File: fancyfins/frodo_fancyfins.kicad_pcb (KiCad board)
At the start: 2 copper layers, 140 x 115 mm, 102 parts, among them J3 TC2050, U1 AZ1117-5.0, U10 L78L05_SOT89, U11 W25Q128JVP, U12 L78L05_SOT89, U13 L78L05_SOT89, U14 L78L05_SOT89, U15 L78L05_SOT89, U16 L78L05_SOT89, U2 AZ1117-3.3, U3 STM32F103RCTx, U4 MCP2562-E-SN, U5 TPD4E1U06, U6 L78L05_SOT89, U7 L78L05_SOT89, U8 L78L05_SOT89, U9 L78L05_SOT89, Y1 8MHz 12pF

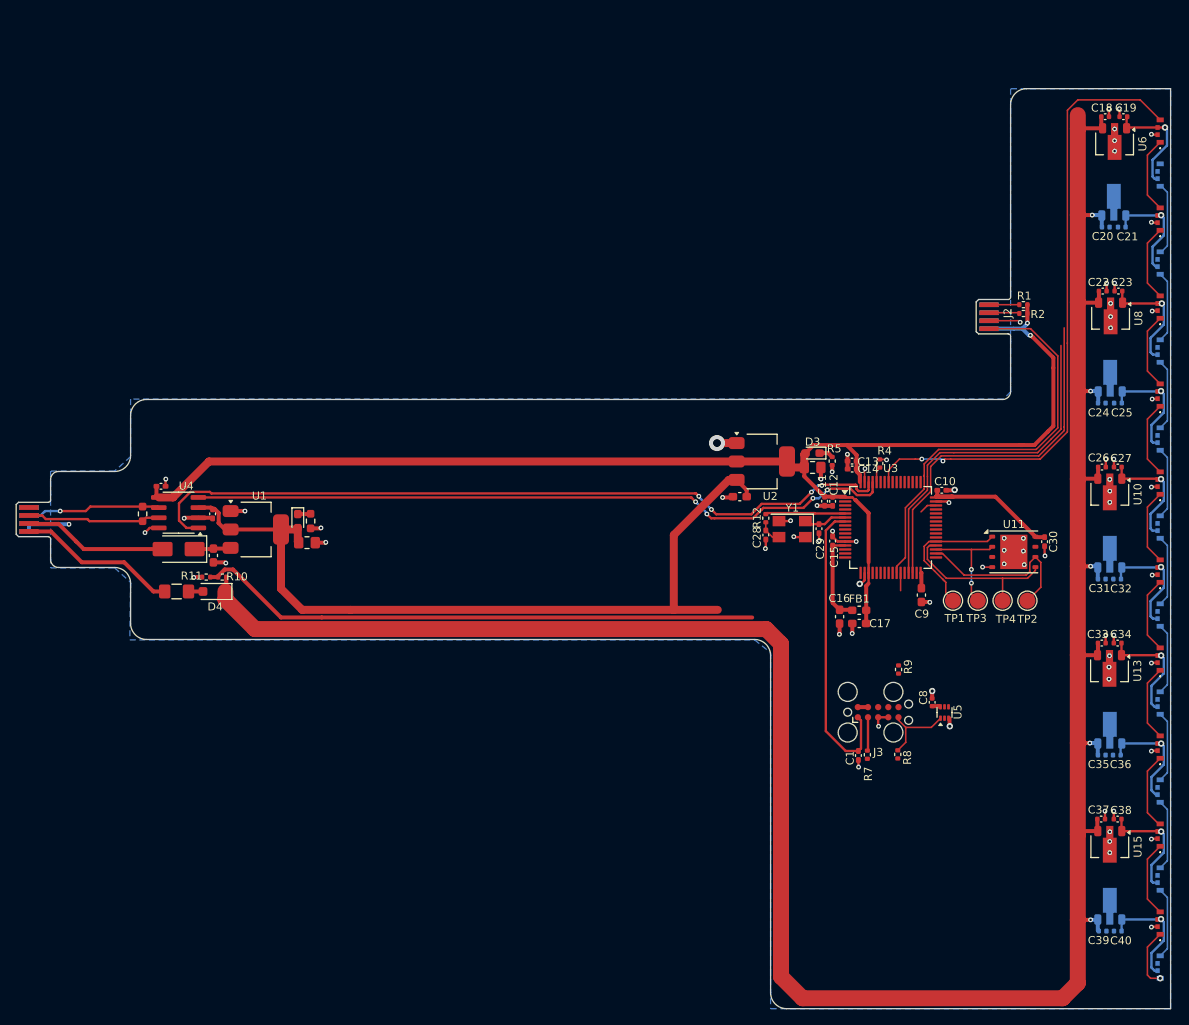
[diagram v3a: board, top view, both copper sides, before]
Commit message: fixed gnd issue
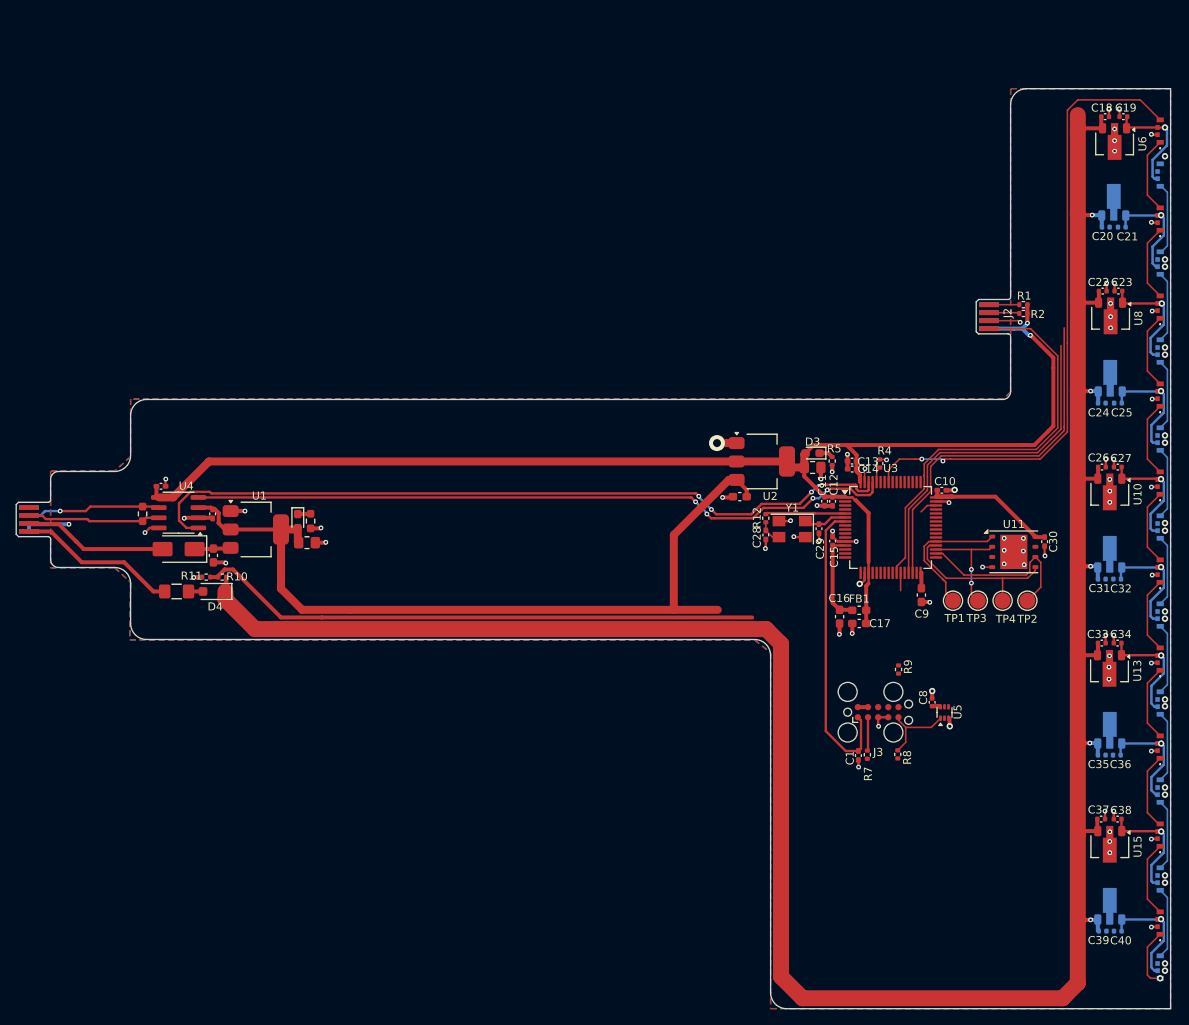
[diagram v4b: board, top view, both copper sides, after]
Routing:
- net GND: vias 77 -> 96
- added copper zone on F.Cu, net GND
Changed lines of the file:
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@@
 	)
 	(via
+		(at 225.3 78.35)
+		(size 0.8)
+		(drill 0.4)
+		(layers "F.Cu" "B.Cu")
+		(free yes)
+		(net 1)
+	)
+	(via
 		(at 169.3 79.3)
 		(size 2)
@@
 	)
 	(via
+		(at 225.3 67.35)
+		(size 0.8)
+		(drill 0.4)
+		(layers "F.Cu" "B.Cu")
+		(free yes)
+		(net 1)
+	)
+	(via
 		(at 223.7 62.8)
 		(size 0.6)
@@
 	)
 	(via
+		(at 225.3 79.25)
+		(size 0.8)
+		(drill 0.4)
+		(layers "F.Cu" "B.Cu")
+		(free yes)
+		(net 1)
+	)
+	(via
 		(at 223.6 139.8)
 		(size 0.6)
@@
 	)
 	(via
+		(at 225.3 101.25)
+		(size 0.8)
+		(drill 0.4)
+		(layers "F.Cu" "B.Cu")
+		(free yes)
+		(net 1)
+	)
+	(via
+		(at 225.3 56.35)
+		(size 0.8)
+		(drill 0.4)
+		(layers "F.Cu" "B.Cu")
+		(free yes)
+		(net 1)
+	)
+	(via
 		(at 218.5 64.9)
 		(size 0.6)
@@
 	)
 	(via
+		(at 225.3 112.2)
+		(size 0.8)
+		(drill 0.4)
+		(layers "F.Cu" "B.Cu")
+		(free yes)
+		(net 1)
+	)
+	(via
 		(at 181.8 87.1)
 		(size 0.6)
@@
 	)
 	(via
+		(at 225.3 122.35)
+		(size 0.8)
+		(drill 0.4)
+		(layers "F.Cu" "B.Cu")
+		(free yes)
+		(net 1)
+	)
+	(via
 		(at 119.8 89.9)
 		(size 0.6)
@@
 	)
 	(via
+		(at 225.3 133.35)
+		(size 0.8)
+		(drill 0.4)
+		(layers "F.Cu" "B.Cu")
+		(free yes)
+		(net 1)
+	)
+	(via
 		(at 218.5 63.5)
 		(size 0.6)
@@
 	)
 	(via
+		(at 225.3 144.35)
+		(size 0.8)
+		(drill 0.4)
+		(layers "F.Cu" "B.Cu")
+		(free yes)
+		(net 1)
+	)
+	(via
 		(at 205.2 94.4)
 		(size 0.6)
@@
 	)
 	(via
+		(at 225.3 134.25)
+		(size 0.8)
+		(drill 0.4)
+		(layers "F.Cu" "B.Cu")
+		(free yes)
+		(net 1)
+	)
+	(via
 		(at 223.6 128.8)
 		(size 0.6)
@@
 	)
 	(via
+		(at 225.3 145.25)
+		(size 0.8)
+		(drill 0.4)
+		(layers "F.Cu" "B.Cu")
+		(free yes)
+		(net 1)
+	)
+	(via
 		(at 100.4 83.8)
 		(size 0.6)
@@
 	)
 	(via
+		(at 225.3 57.25)
+		(size 0.8)
+		(drill 0.4)
+		(layers "F.Cu" "B.Cu")
+		(free yes)
+		(net 1)
+	)
+	(via
 		(at 207.6 92.8)
 		(size 0.6)
@@
 	)
 	(via
+		(at 225.3 111.35)
+		(size 0.8)
+		(drill 0.4)
+		(layers "F.Cu" "B.Cu")
+		(free yes)
+		(net 1)
+	)
+	(via
 		(at 223.7 73.8)
 		(size 0.6)
@@
 	)
 	(via
+		(at 225.3 89.3)
+		(size 0.8)
+		(drill 0.4)
+		(layers "F.Cu" "B.Cu")
+		(free yes)
+		(net 1)
+	)
+	(via
 		(at 107.9 94.3)
 		(size 0.6)
@@
 	)
 	(via
+		(at 225.3 43.45)
+		(size 0.8)
+		(drill 0.4)
+		(layers "F.Cu" "B.Cu")
+		(free yes)
+		(net 1)
+	)
+	(via
 		(at 218.9 81.3)
 		(size 0.6)
@@
 	)
 	(via
+		(at 225.3 100.35)
+		(size 0.8)
+		(drill 0.4)
+		(layers "F.Cu" "B.Cu")
+		(free yes)
+		(net 1)
+	)
+	(via
 		(at 189.5 114.7)
 		(size 0.6)
@@
 	)
 	(via
+		(at 225.3 68.25)
+		(size 0.8)
+		(drill 0.4)
+		(layers "F.Cu" "B.Cu")
+		(free yes)
+		(net 1)
+	)
+	(via
 		(at 207.6 91.2)
 		(size 0.6)
@@
 	)
 	(via
+		(at 225.3 123.25)
+		(size 0.8)
+		(drill 0.4)
+		(layers "F.Cu" "B.Cu")
+		(free yes)
+		(net 1)
+	)
+	(via
+		(at 225.3 90.25)
+		(size 0.8)
+		(drill 0.4)
+		(layers "F.Cu" "B.Cu")
+		(free yes)
+		(net 1)
+	)
+	(via
 		(at 218.4 130.5)
 		(size 0.6)
@@
 		(net 1)
 		(net_name "GND")
+		(layer "F.Cu")
+		(hatch edge 0.5)
+		(priority 1)
+		(connect_pads
+			(clearance 0.25)
+		)
+		(min_thickness 0.25)
+		(filled_areas_thickness no)
+		(fill yes
+			(thermal_gap 0.5)
+			(thermal_bridge_width 0.5)
+			(island_removal_mode 2)
+			(island_area_min 1)
+		)
+		(polygon
+			(pts
+				(xy 86 82.8) (xy 86 94.9) (xy 94 94.85) (xy 96 96.7) (xy 95.9 103.9) (xy 174 103.9) (xy 176 105.5)
+				(xy 176 150) (xy 226.001 150) (xy 226.001 35) (xy 206 35) (xy 206 72.9) (xy 205.1 73.8) (xy 96 73.8)
+				(xy 96 81) (xy 94 82.8)
+			)
+		)
+	)
+	(zone
+		(net 1)
+		(net_name "GND")
 		(layer "B.Cu")
 		(hatch edge 0.5)
 		(connect_pads yes
-			(clearance 0.35)
+			(clearance 0.25)
 		)
 		(min_thickness 0.25)
@@
 			(thermal_gap 0.5)
 			(thermal_bridge_width 0.5)
+			(island_removal_mode 2)
+			(island_area_min 1)
 		)
 		(polygon

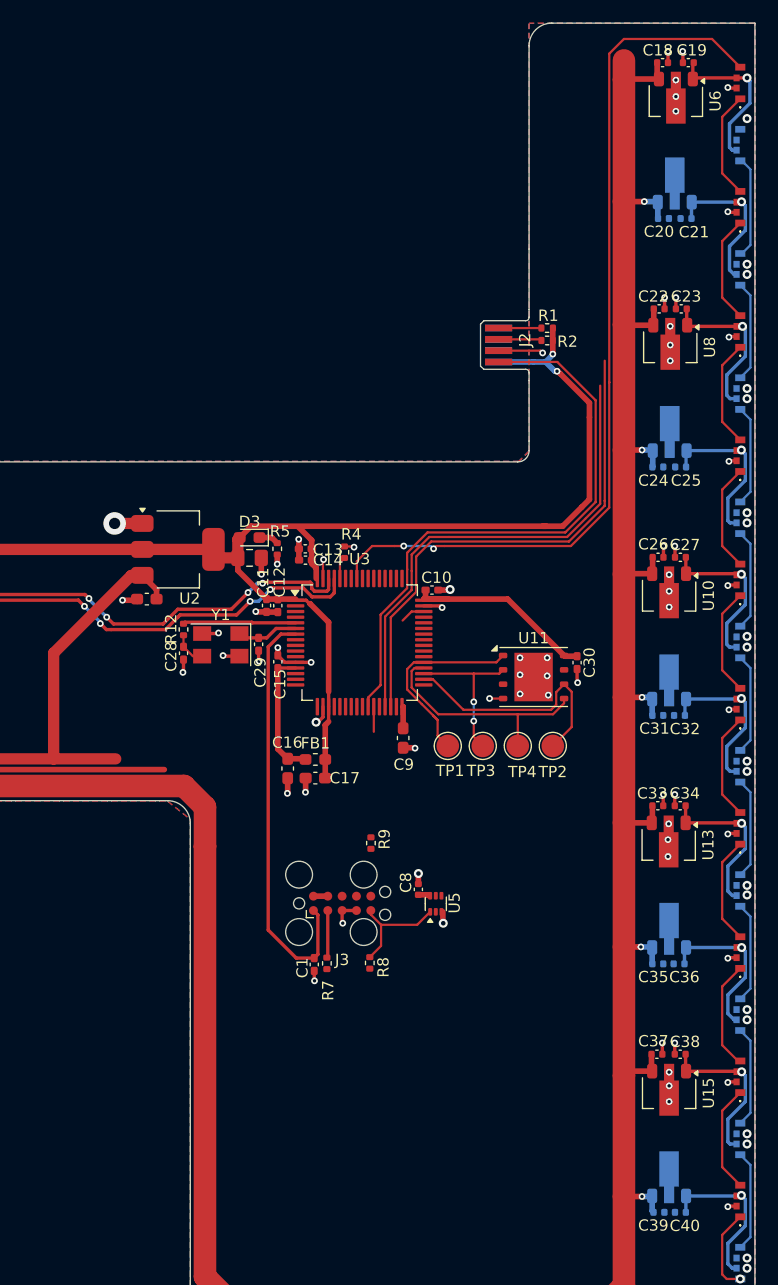
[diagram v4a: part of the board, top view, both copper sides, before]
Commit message: added some vias for better gnd connection
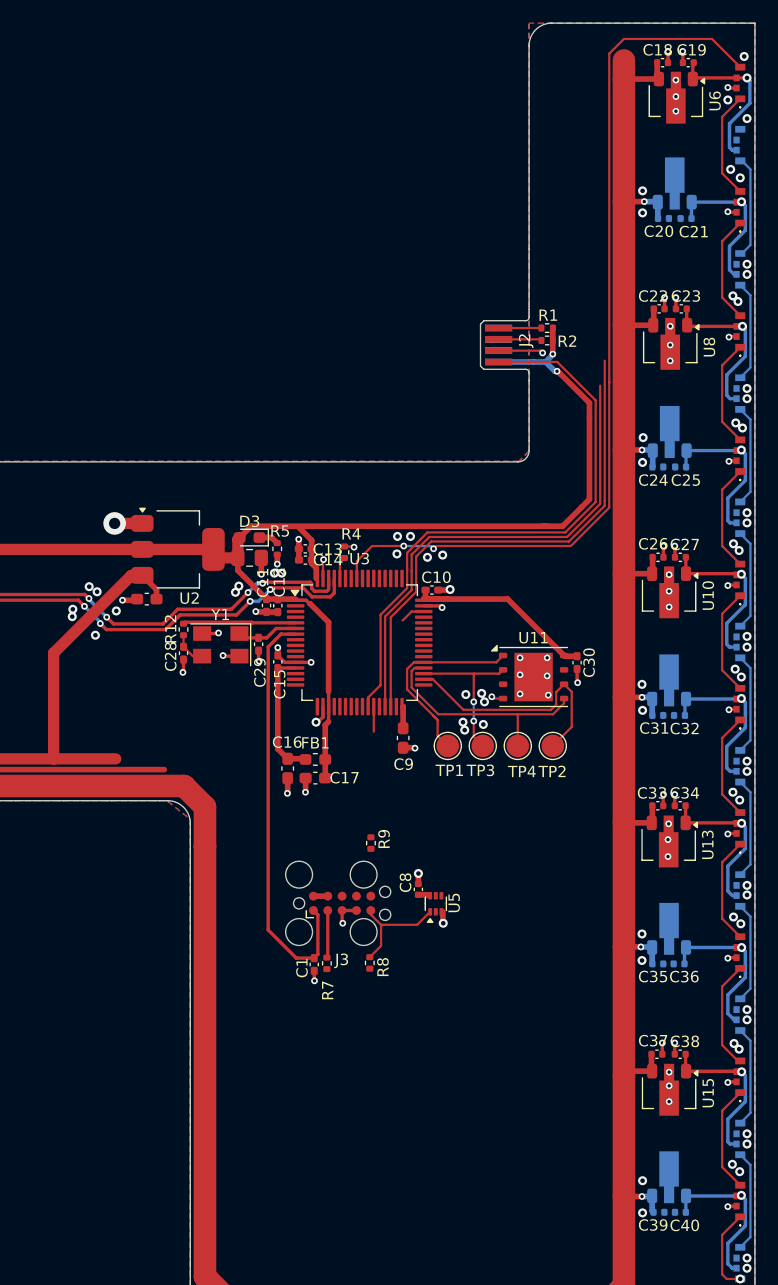
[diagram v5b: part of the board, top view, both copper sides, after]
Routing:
- net GND: track 78.7 -> 78.6 mm, vias 96 -> 147

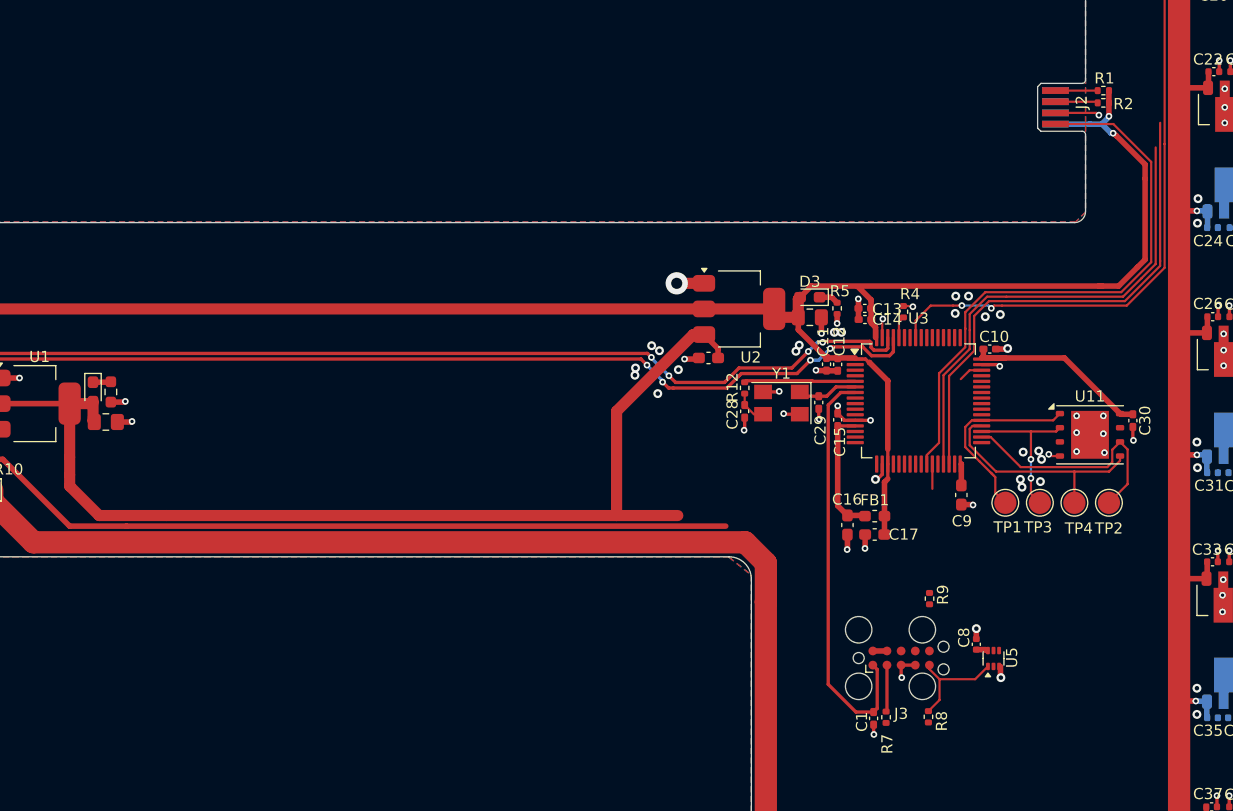
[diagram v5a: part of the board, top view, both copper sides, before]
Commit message: finalized fancyfin routing (for now)
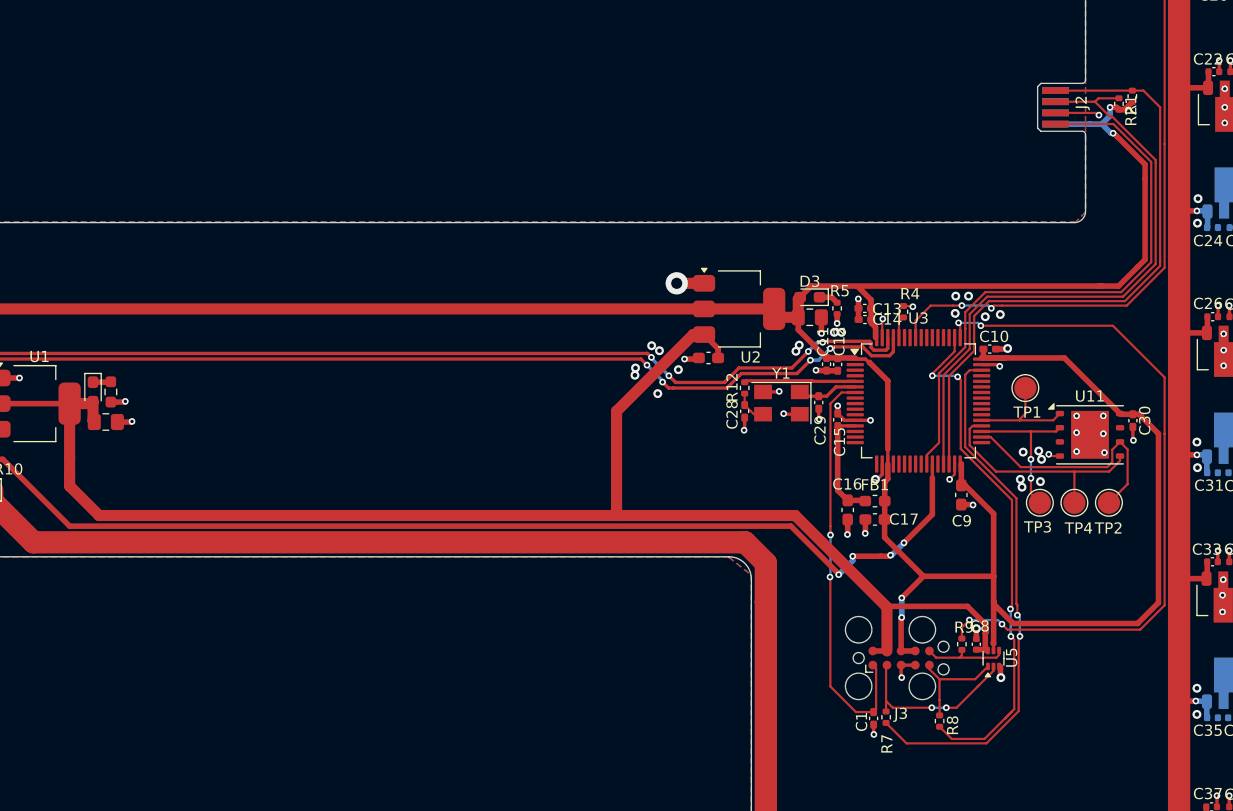
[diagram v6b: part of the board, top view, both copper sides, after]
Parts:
- moved TP1 10.5 mm to (200.6, 88.7)
- moved R9 5.02 mm to (194.9, 111.7)
- moved R2 2.67 mm to (210.2, 62.5), turned to 90 degrees
- moved R1 1.84 mm to (209.0, 63.2), turned to 90 degrees
- moved FB1 1.35 mm to (187.1, 98.8)
- moved C16 1.35 mm to (184.7, 99.7)
- moved C17 1.35 mm to (187.1, 100.5)
- moved R8 1.08 mm to (192.9, 118.6)
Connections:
- J2 pad 1: P_SCL -> P_SDA
- J2 pad 2: P_SDA -> P_SCL
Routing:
- net +3.3V: track 190.5 -> 262.8 mm, vias 2 -> 4
- net SWCLK: track 0.00 -> 63.1 mm, vias 0 -> 4
- net SWO: track 0.00 -> 47.8 mm, vias 0 -> 4
- net SWDIO: track 2.21 -> 47.8 mm, vias 0 -> 2
- net +5V: track 104.3 -> 142.2 mm
- net VDsense: track 72.9 -> 98.1 mm, vias 0 -> 4
- net /J1-SWDIO: track 4.20 -> 16.0 mm, vias 0 -> 2
- net P_SCL: track 47.4 -> 55.8 mm
- net Net-(J3-Pin_6): track 0.00 -> 7.78 mm
- net P_SDA: track 49.5 -> 57.2 mm
- net SPI_CS_FLASH: track 17.6 -> 10.4 mm
- net GND: track 78.6 -> 80.1 mm, vias 147 -> 148
- net +3.3VA: track 11.6 -> 10.2 mm
- net NRST: track 37.6 -> 37.3 mm, vias 0 -> 2
